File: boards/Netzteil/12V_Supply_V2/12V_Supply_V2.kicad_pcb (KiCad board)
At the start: 2 copper layers, 90 x 66 mm, 54 parts, among them P1 12V_AC, P2 12V_DC_1, P3 12V_DC_2, P4 Relais, P5 12V_DC_3, P6 12V_DC_4, P7 Relais, Q1 BS170, U1 LM393, U2 LM7812CT

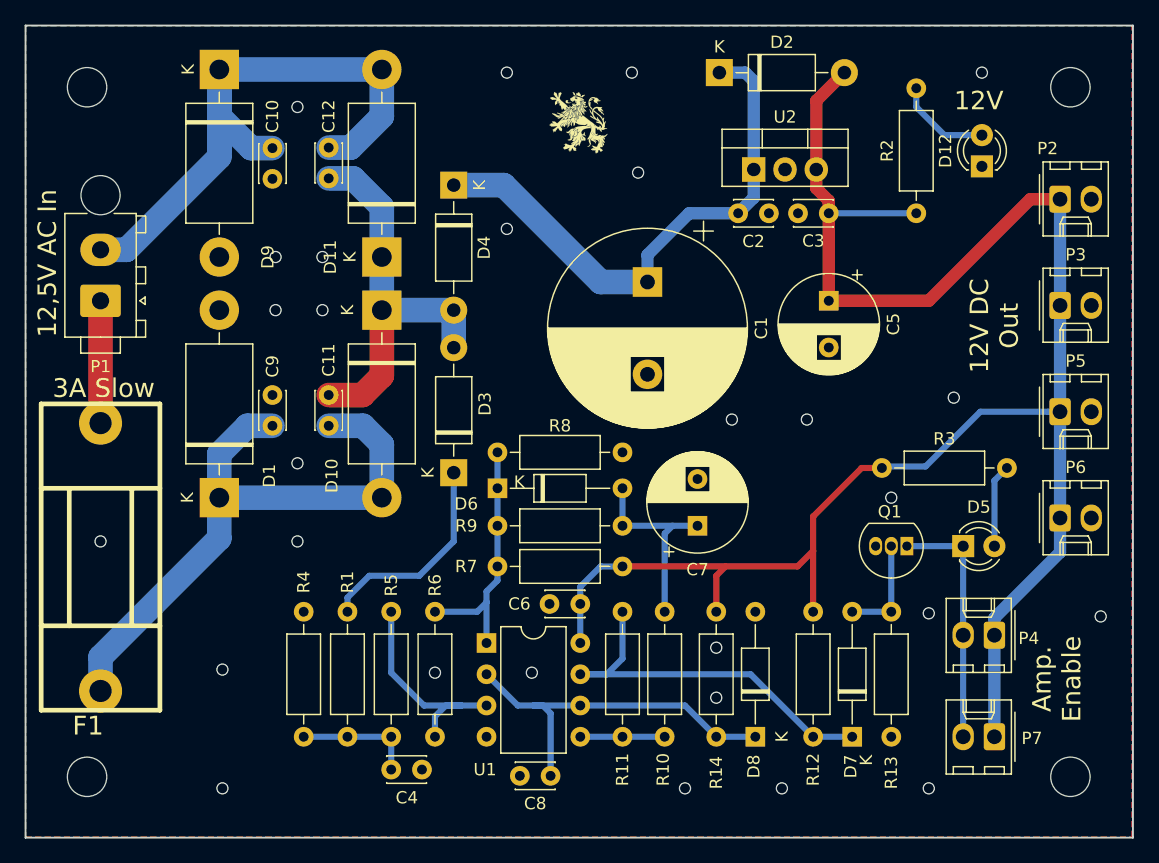
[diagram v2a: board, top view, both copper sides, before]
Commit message: Added Mounting holes, Moved -60V Divider to HV Board, eliminated +450V Connector and Feedback Connector on Amp Board
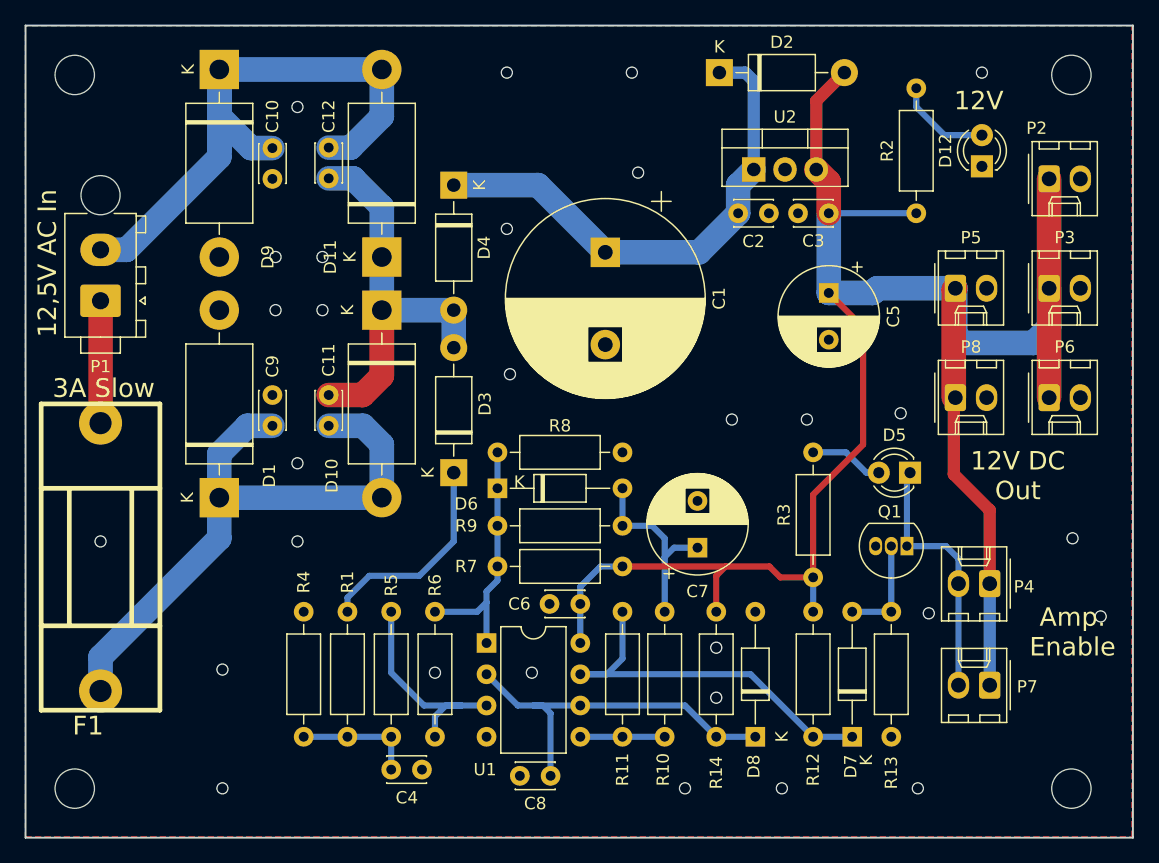
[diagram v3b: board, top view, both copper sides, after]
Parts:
- removed G***: LOGO, Loewe:Loewe_Klein
- removed the REF** at (95.2, 52.2)
- removed the REF** at (175.1, 52.2)
- removed the REF** at (175.1, 108.3)
- removed the REF** at (95.2, 108.3)
- added P8: 12V_DC_4, Connector_Molex:Molex_KK-254_AE-6410-02A_1x02_P2.54mm_Vertical, F.Cu at (165.7, 77.5)
- added REF**: MountingHole_3.2mm_M3_DIN965, MountingHole:MountingHole_3.2mm_M3_DIN965, F.Cu at (94.2, 109.2)
- added REF**: MountingHole_3.2mm_M3_DIN965, MountingHole:MountingHole_3.2mm_M3_DIN965, F.Cu at (175.2, 109.2)
- added REF**: MountingHole_3.2mm_M3_DIN965, MountingHole:MountingHole_3.2mm_M3_DIN965, F.Cu at (175.2, 51.2)
- added REF**: MountingHole_3.2mm_M3_DIN965, MountingHole:MountingHole_3.2mm_M3_DIN965, F.Cu at (94.2, 51.2)
- moved P5 13.2 mm to (165.7, 68.6)
- moved R3 10.5 mm to (154.2, 92.1), turned to 90 degrees
- moved P6 9.82 mm to (173.4, 77.5)
- moved D5 7.37 mm to (162.1, 83.6), turned to 180 degrees
- moved P4 4.21 mm to (168.5, 92.6)
- moved P7 4.21 mm to (168.5, 100.8)
- moved C1 4.19 mm to (137.3, 65.7)
- moved P2 1.88 mm to (173.4, 59.7)
- moved C7 1.78 mm to (144.8, 89.7)
- moved P3 1.66 mm to (173.4, 68.6)
- moved C5 0.64 mm to (155.4, 69.0)
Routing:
- net +12V: track 155.2 -> 160.8 mm
- net Net-(C1-Pad1): track 44.3 -> 41.2 mm
- net Net-(D5-Pad1): track 20.1 -> 21.0 mm
- net Net-(D5-Pad2): track 6.77 -> 6.02 mm
- net Net-(C7-Pad1): track 16.4 -> 15.8 mm
- net GND: vias 28 -> 29
